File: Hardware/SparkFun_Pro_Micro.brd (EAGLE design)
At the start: 17.8 x 37.3 mm, 33 parts, among them J1 USB-A-H, U2 MIC5219, U3 ATMEGA32U4, Y1 16MHz

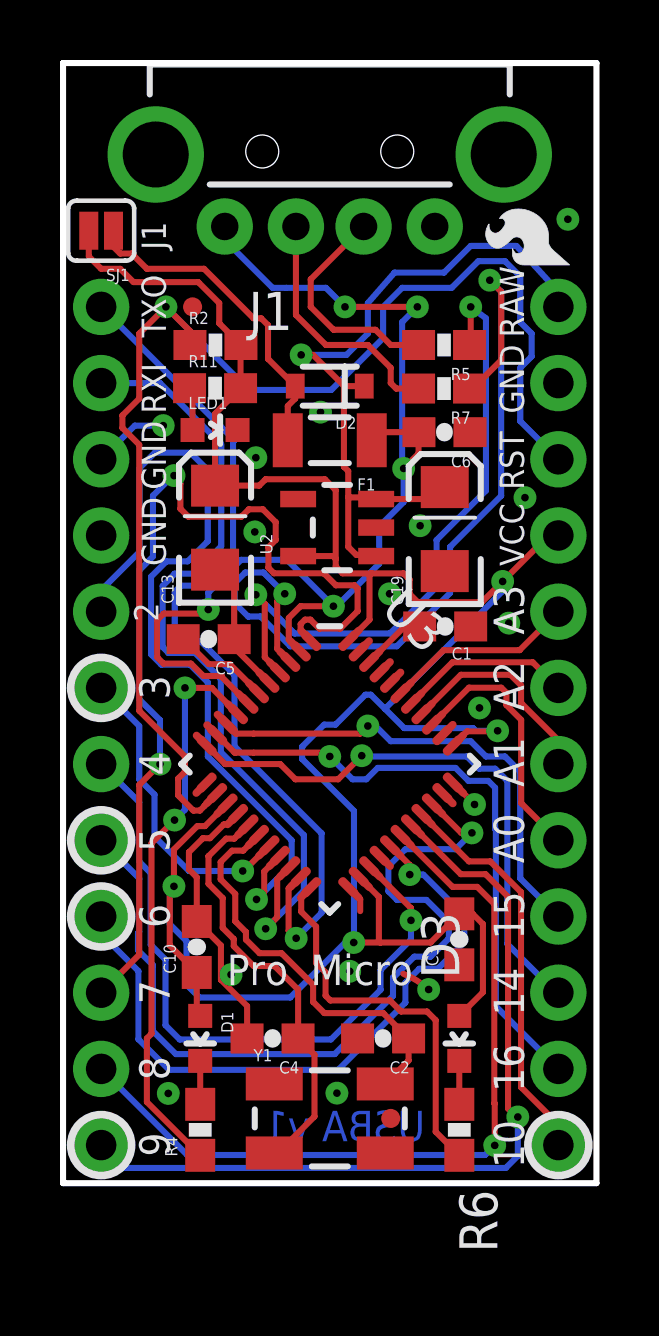
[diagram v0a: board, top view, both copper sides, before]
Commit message: Move top board edge inwards to clear USB-A jack
On version 1.0 the jack doesn't *quite* fit without a little sanding. It turns out that the footprint's silkscreen marker for the top of the board clearance area is off by 0.1 mm (3 mm in the footprint, 2.9 mm in the datasheet), and my board edge followed the grid so it was 0.05 mm past even that. This commit pulls the board edge back to properly accomodate the connector.

Now according to the datasheet the lower edge of the connector is 18.8 mm from the tip, with the mounting tabs 2 mm long. Because the origin of the footprint is the center of these mounting tabs, that makes the origin 17.8 mm offset from the tip. The end of the cutout area is given as 14.90 +/- 0.2 from the tip, which is an offset of 2.9 +/- 0.2 from the footprint origin. Accordingly I set the top board edge to 2.7 mm above the USB footprint's origin to provide clearance up to the max provided tolerance.

Science! ...that I should have probably done the first time around.
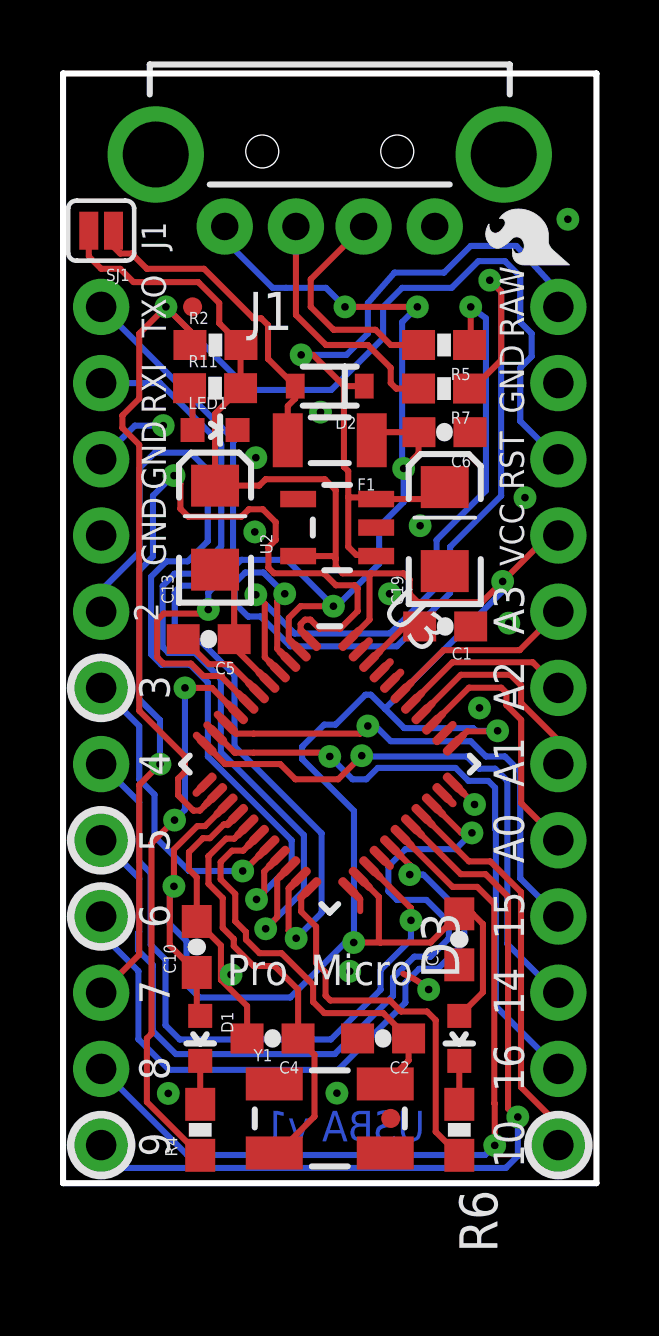
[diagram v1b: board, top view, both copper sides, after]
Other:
- board size 17.8 x 37.3 mm -> 17.8 x 37 mm
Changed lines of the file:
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@@
 <board>
 <plain>
-<wire x1="0" y1="37.338" x2="0" y2="0" width="0.2032" layer="20"/>
+<wire x1="0" y1="36.99" x2="0" y2="0" width="0.2032" layer="20"/>
 <wire x1="0" y1="0" x2="17.78" y2="0" width="0.2032" layer="20"/>
-<wire x1="17.78" y1="0" x2="17.78" y2="37.338" width="0.2032" layer="20"/>
-<wire x1="17.78" y1="37.338" x2="0" y2="37.338" width="0.2032" layer="20"/>
+<wire x1="17.78" y1="0" x2="17.78" y2="36.99" width="0.2032" layer="20"/>
+<wire x1="17.78" y1="36.99" x2="0" y2="36.99" width="0.2032" layer="20"/>
 <wire x1="15.494" y1="0.508" x2="15.494" y2="29.21" width="0.0762" layer="51"/>
 <wire x1="3.556" y1="0.508" x2="3.556" y2="28.956" width="0.0762" layer="51"/>
@@
 <via x="12.186921875" y="6.456678125" extent="1-16" drill="0.254"/>
 <polygon width="0.254" layer="1" isolate="0.2032">
-<vertex x="0" y="37.338"/>
-<vertex x="17.78" y="37.338"/>
+<vertex x="0" y="36.99"/>
+<vertex x="17.78" y="36.99"/>
 <vertex x="17.78" y="0"/>
 <vertex x="0" y="0"/>
 </polygon>
 <polygon width="0.254" layer="16" isolate="0.2032">
-<vertex x="0" y="37.338"/>
-<vertex x="17.78" y="37.338"/>
+<vertex x="0" y="36.99"/>
+<vertex x="17.78" y="36.99"/>
 <vertex x="17.78" y="0"/>
 <vertex x="0" y="0"/>
